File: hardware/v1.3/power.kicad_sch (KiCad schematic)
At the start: 48 parts, among them U1 ECP5-CABGA256, U2 TLV62569DBV, U3 TLV62569DBV, U4 TLV62569DBV

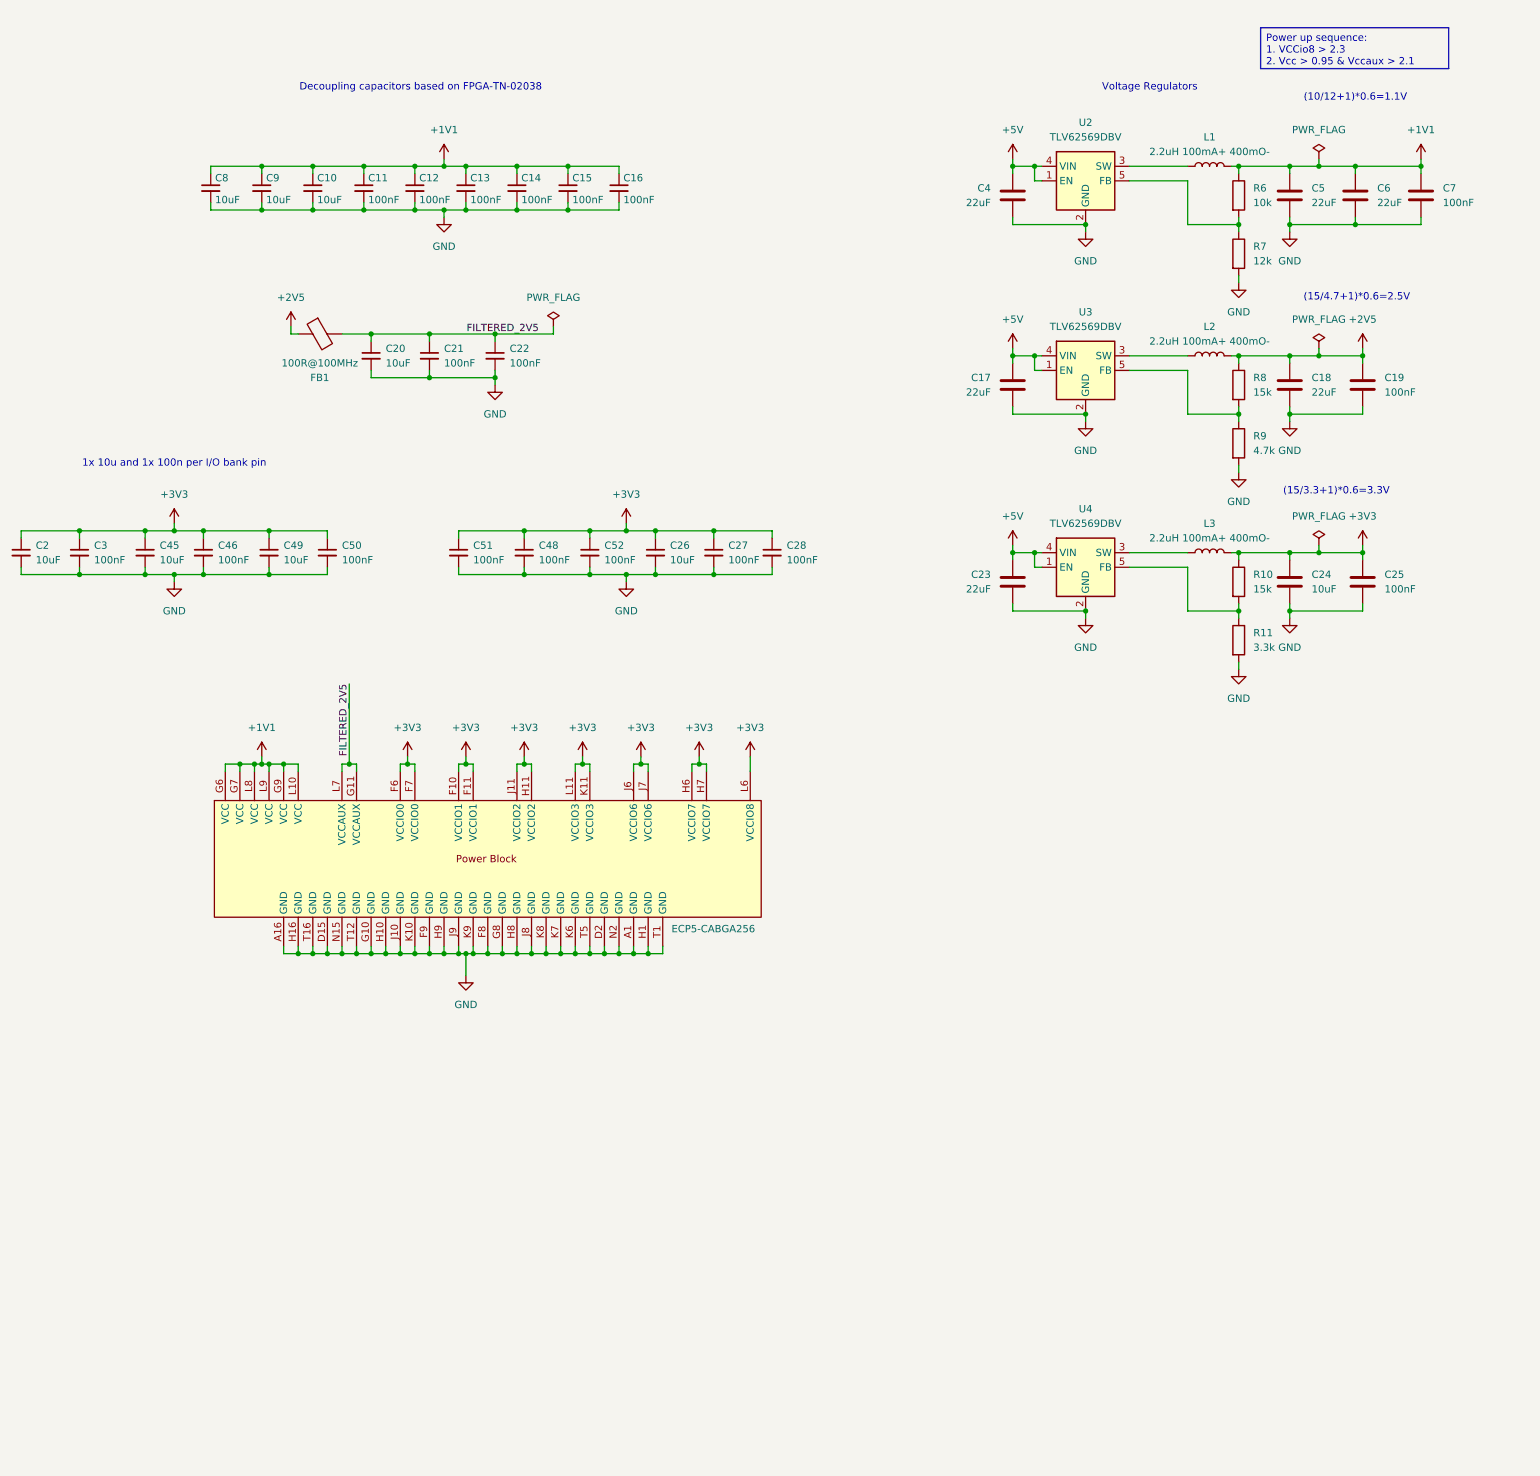
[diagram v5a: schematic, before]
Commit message: Improve makefile and hardware
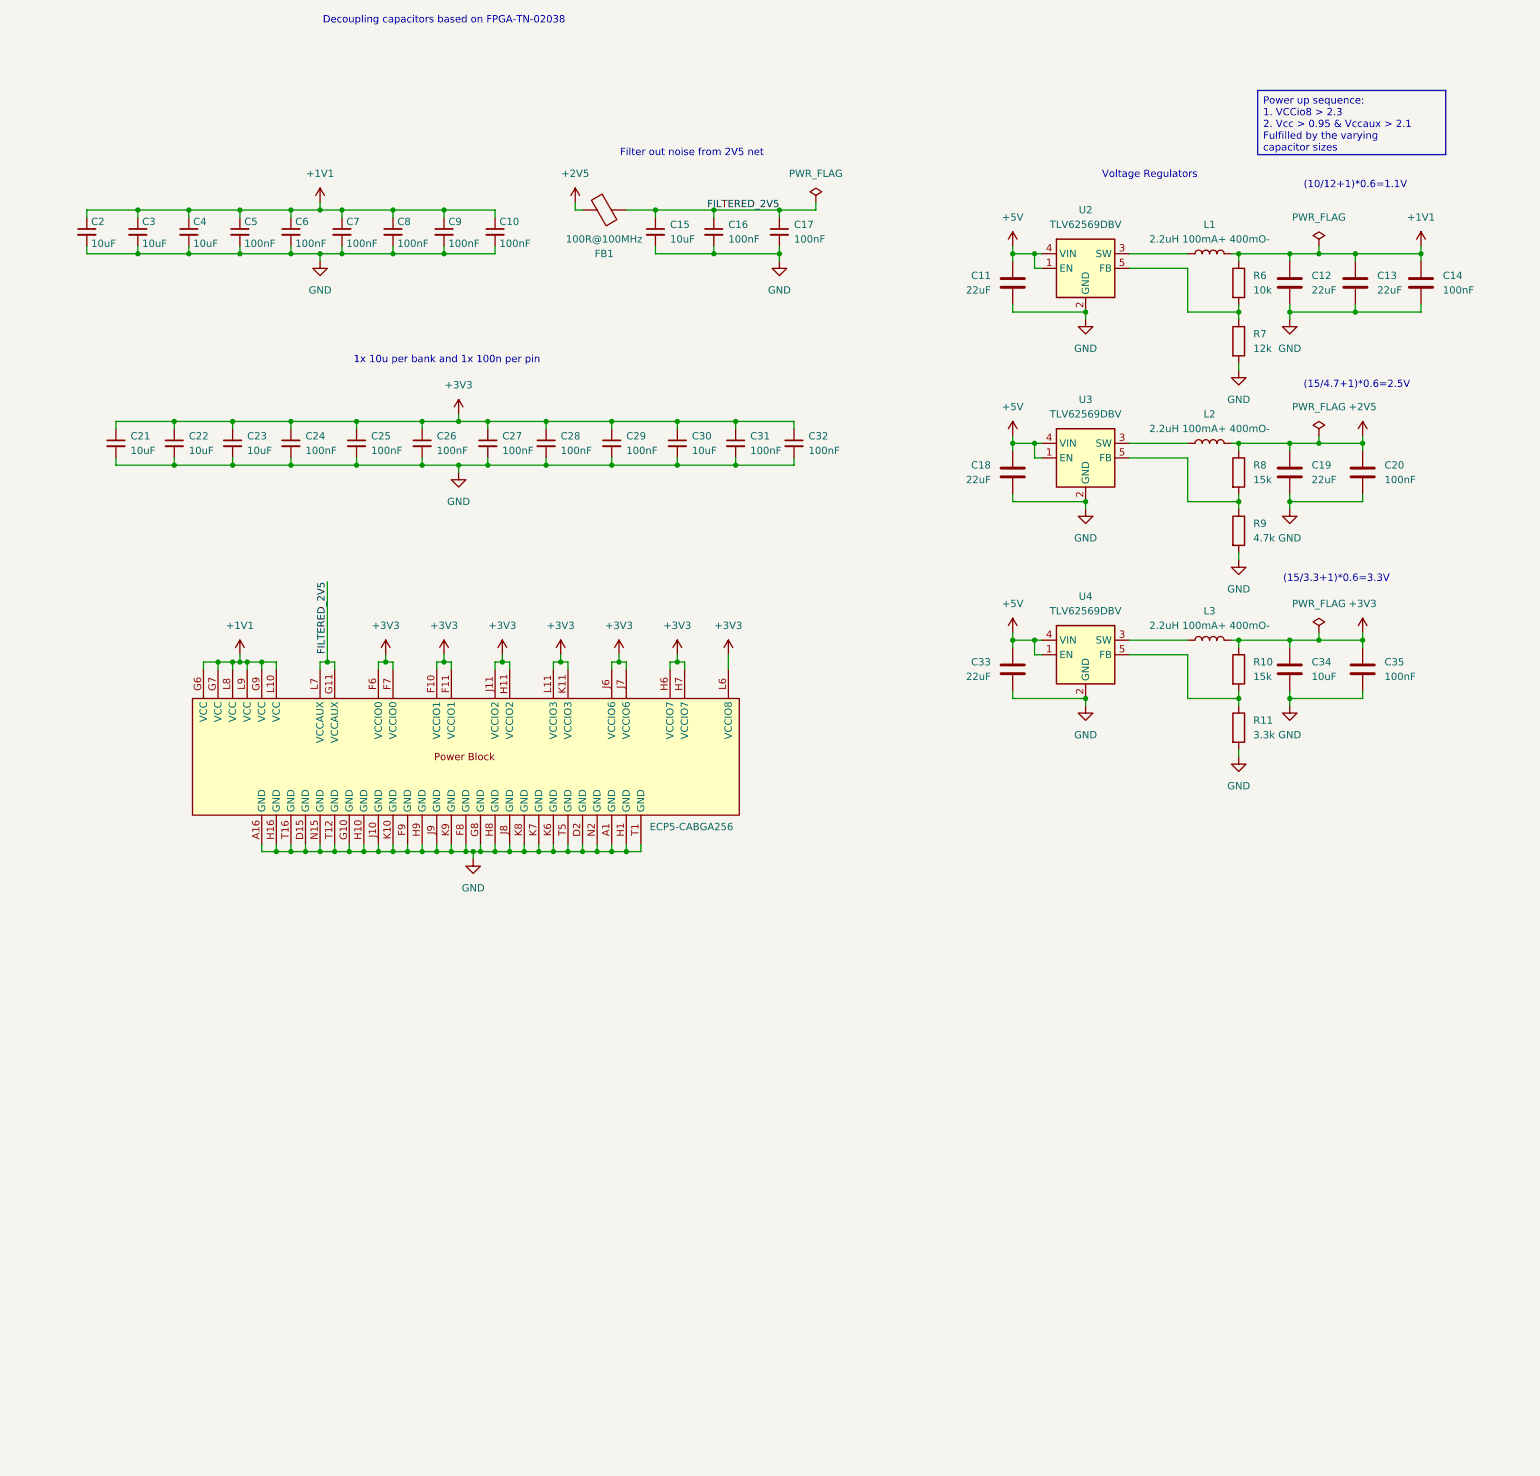
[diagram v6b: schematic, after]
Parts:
- renumbered C16 to C10, C4 to C11, C5 to C12, C6 to C13, C7 to C14, C20 to C15, C21 to C16, C22 to C17, C17 to C18, C18 to C19, C8 to C2, C19 to C20, C2 to C21, C45 to C22, C49 to C23, C3 to C24, C46 to C25, C50 to C26, C51 to C27, C48 to C28, C52 to C29, C9 to C3, C26 to C30, C27 to C31, C28 to C32, C23 to C33, C24 to C34, C25 to C35, C10 to C4, C11 to C5, C12 to C6, C13 to C7, C14 to C8, C15 to C9
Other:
- note added: "1x 10u per bank and 1x 100n per pin"
- note added: "Filter out noise from 2V5 net"
- note removed: "1x 10u and 1x 100n per I/O bank pin"
- title: Icepi zero -> Icepi Zero
- moved on the sheet: C10, C11, C12, C13, C14, C15, C16, C17, C18, C19, C2, C20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

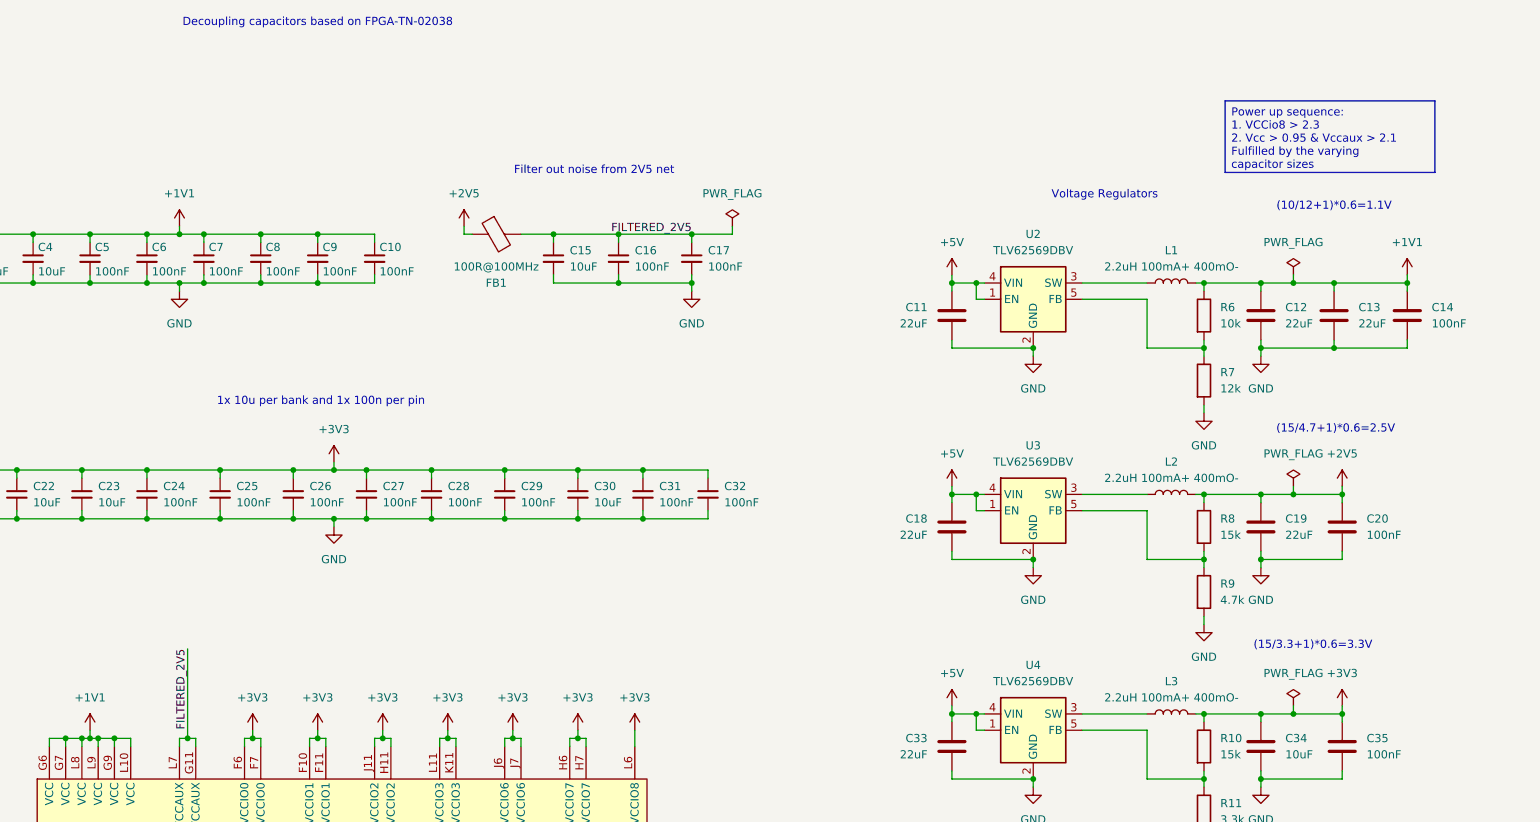
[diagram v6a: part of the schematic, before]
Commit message: Fix typo in readme
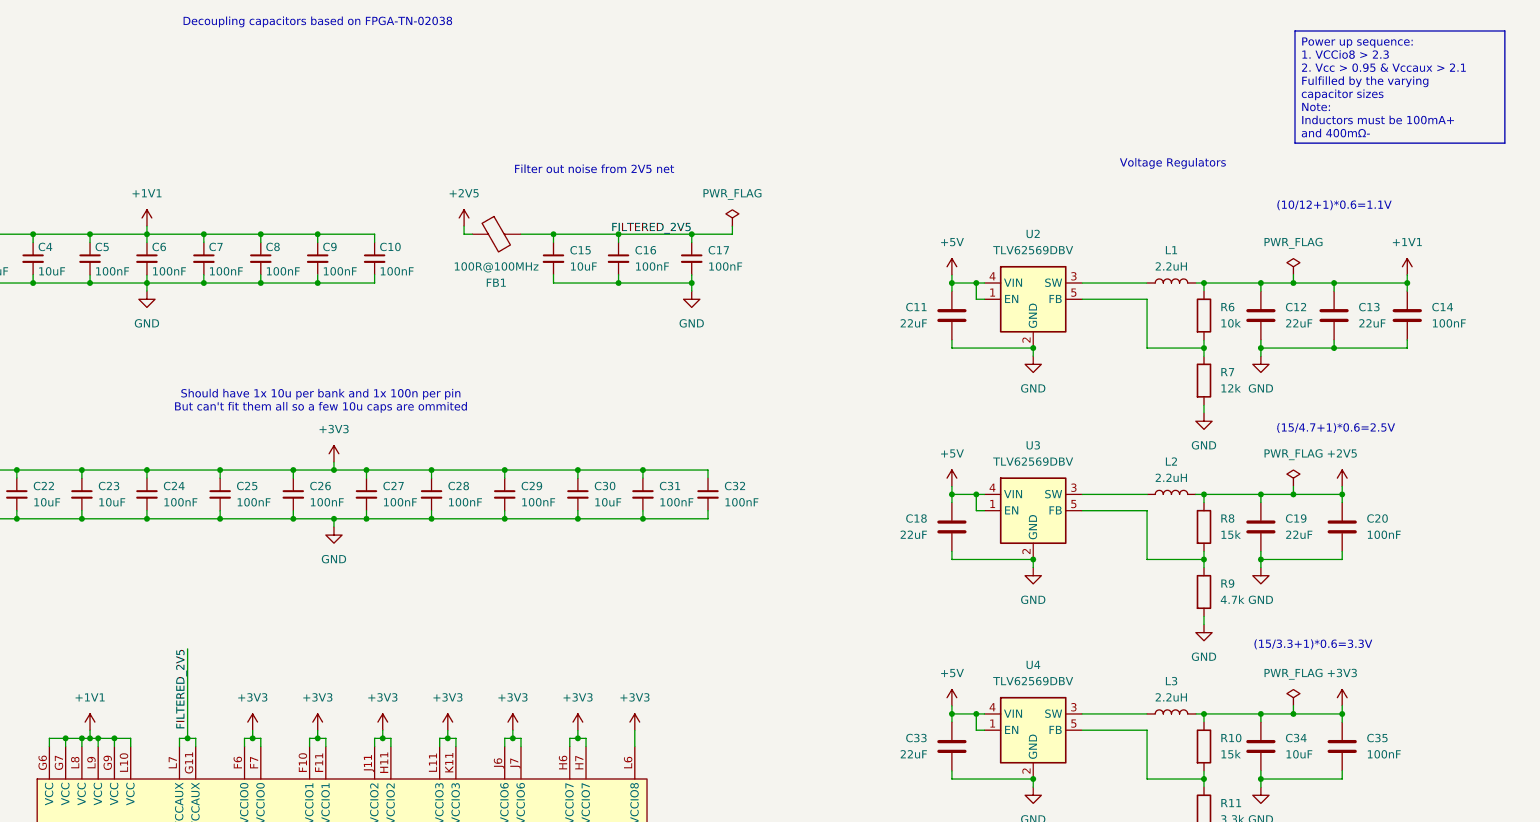
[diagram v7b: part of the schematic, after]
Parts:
- L1, L2, L3: value 2.2uH 100mA+ 400mO- -> 2.2uH
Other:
- note added: "Should have 1x 10u per bank and 1x 100n per pin But can't fit them all so a few 10u caps are ommited"
- note removed: "1x 10u per bank and 1x 100n per pin"
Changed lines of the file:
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@@
 		)
 	)
-	(text "1x 10u per bank and 1x 100n per pin"
+	(text "Should have 1x 10u per bank and 1x 100n per pin\nBut can't fit them all so a few 10u caps are ommited"
 		(exclude_from_sim no)
 		(at 97.028 73.152 0)
@@
 	(text "Voltage Regulators"
 		(exclude_from_sim no)
-		(at 219.456 40.894 0)
+		(at 230.124 36.068 0)
 		(effects
 			(font
@@
 		)
 	)
-	(text_box "Power up sequence:\n1. VCCio8 > 2.3\n2. Vcc > 0.95 & Vccaux > 2.1\nFulfilled by the varying capacitor sizes"
+	(text_box "Power up sequence:\n1. VCCio8 > 2.3\n2. Vcc > 0.95 & Vccaux > 2.1\nFulfilled by the varying capacitor sizes\nNote:\nInductors must be 100mA+ and 400mΩ-"
 		(exclude_from_sim no)
-		(at 238.252 26.162 0)
-		(size 32.766 11.176)
+		(at 249.174 15.24 0)
+		(size 32.766 17.526)
 		(margins 0.9525 0.9525 0.9525 0.9525)
 		(stroke
@@
 	)
 	(junction
-		(at 74.93 54.61)
-		(diameter 0)
-		(color 0 0 0 0)
-	)
-	(junction
 		(at 62.23 125.73)
 		(diameter 0)
@@
 	)
 	(junction
-		(at 74.93 46.99)
-		(diameter 0)
-		(color 0 0 0 0)
-	)
-	(junction
 		(at 60.96 46.99)
 		(diameter 0)
@@
 	(wire
 		(pts
-			(xy 74.93 46.99) (xy 69.85 46.99)
+			(xy 69.85 46.99) (xy 78.74 46.99)
 		)
 		(stroke
@@
 	(wire
 		(pts
+			(xy 69.85 54.61) (xy 78.74 54.61)
+		)
+		(stroke
+			(width 0)
+			(type default)
+		)
+	)
+	(wire
+		(pts
 			(xy 256.54 121.92) (xy 248.92 121.92)
 		)
@@
 	(wire
 		(pts
-			(xy 74.93 54.61) (xy 78.74 54.61)
-		)
-		(stroke
-			(width 0)
-			(type default)
-		)
-	)
-	(wire
-		(pts
 			(xy 243.84 55.88) (xy 243.84 54.61)
 		)
@@
 	(wire
 		(pts
-			(xy 74.93 45.72) (xy 74.93 46.99)
+			(xy 69.85 45.72) (xy 69.85 46.99)
 		)
 		(stroke
@@
 	(wire
 		(pts
-			(xy 78.74 46.99) (xy 74.93 46.99)
-		)
-		(stroke
-			(width 0)
-			(type default)
-		)
-	)
-	(wire
-		(pts
 			(xy 243.84 99.06) (xy 243.84 97.79)
 		)
@@
 	(wire
 		(pts
-			(xy 69.85 54.61) (xy 74.93 54.61)
-		)
-		(stroke
-			(width 0)
-			(type default)
-		)
-	)
-	(wire
-		(pts
 			(xy 72.39 157.48) (xy 72.39 158.75)
 		)
@@
 	(wire
 		(pts
-			(xy 74.93 54.61) (xy 74.93 55.88)
+			(xy 69.85 54.61) (xy 69.85 55.88)
 		)
 		(stroke
@@
 			)
 		)
-		(property "Value" "2.2uH 100mA+ 400mO-"
+		(property "Value" "2.2uH"
 			(at 229.87 119.38 90)
 			(effects
@@
 			)
 		)
-		(property "Value" "2.2uH 100mA+ 400mO-"
+		(property "Value" "2.2uH"
 			(at 229.87 52.07 90)
 			(effects
@@
 	(symbol
 		(lib_id "power:+1V1")
-		(at 74.93 45.72 0)
+		(at 69.85 45.72 0)
 		(unit 1)
 		(exclude_from_sim no)
@@
 		(fields_autoplaced yes)
 		(property "Reference" "#PWR024"
-			(at 74.93 49.53 0)
+			(at 69.85 49.53 0)
 			(effects
 				(font
@@
 		)
 		(property "Value" "+1V1"
-			(at 74.93 40.64 0)
+			(at 69.85 40.64 0)
 			(effects
 				(font
@@
 		)
 		(property "Footprint" ""
-			(at 74.93 45.72 0)
+			(at 69.85 45.72 0)
 			(effects
 				(font
@@
 		)
 		(property "Datasheet" ""
-			(at 74.93 45.72 0)
+			(at 69.85 45.72 0)
 			(effects
 				(font
@@
 		)
 		(property "Description" "Power symbol creates a global label with name \"+1V1\""
-			(at 74.93 45.72 0)
+			(at 69.85 45.72 0)
 			(effects
 				(font
@@
 	(symbol
 		(lib_id "power:GND")
-		(at 74.93 55.88 0)
+		(at 69.85 55.88 0)
 		(unit 1)
 		(exclude_from_sim no)
@@
 		(fields_autoplaced yes)
 		(property "Reference" "#PWR025"
-			(at 74.93 62.23 0)
+			(at 69.85 62.23 0)
 			(effects
 				(font
@@
 		)
 		(property "Value" "GND"
-			(at 74.93 60.96 0)
+			(at 69.85 60.96 0)
 			(effects
 				(font
@@
 		)
 		(property "Footprint" ""
-			(at 74.93 55.88 0)
+			(at 69.85 55.88 0)
 			(effects
 				(font
@@
 		)
 		(property "Datasheet" ""
-			(at 74.93 55.88 0)
+			(at 69.85 55.88 0)
 			(effects
 				(font
@@
 		)
 		(property "Description" "Power symbol creates a global label with name \"GND\" , ground"
-			(at 74.93 55.88 0)
+			(at 69.85 55.88 0)
 			(effects
 				(font
@@
 			)
 		)
-		(property "Value" "2.2uH 100mA+ 400mO-"
+		(property "Value" "2.2uH"
 			(at 229.87 85.09 90)
 			(effects
